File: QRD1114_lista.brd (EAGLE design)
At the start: 66 x 21 mm, 17 parts

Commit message: Add files via upload
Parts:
- removed LED1: (no value), led:CHIPLED-0603-TTW
- added LED: (no value), led:CHIPLED-0603-TTW
- added R11: 330, resistor:R0805
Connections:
- new net N$3: LED.A@1, R11.1
- net +5V: now also R11.2; no longer LED1.A@1
- net GND: now also LED.C@1; no longer LED1.C@1
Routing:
- net N$3: track 0.00 -> 9.73 mm
- net GND: track 72.7 -> 69.3 mm
- net S2: track 22.0 -> 20.8 mm
- net +5V: track 84.0 -> 84.6 mm
- net S1: track 30.1 -> 29.5 mm

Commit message: Add files via upload
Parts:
- LED: device led:CHIPLED-0603-TTW -> led:SML0603
- R11: device resistor:R0805 -> resistor:R0603
- moved R11 5.10 mm to (53.2, 11.0)
- moved R1 3.00 mm to (73.5, 9.00)
- moved R10 3.00 mm to (26.5, 9.00)
- moved R2 3.00 mm to (76.5, 9.00)
- moved R3 3.00 mm to (61.5, 4.00)
- moved R4 3.00 mm to (58.5, 4.00)
- moved R5 3.00 mm to (48.5, 4.00)
- moved R6 3.00 mm to (51.5, 4.00)
- moved R7 3.00 mm to (41.5, 4.00)
- moved R8 3.00 mm to (38.5, 4.00)
- moved R9 3.00 mm to (23.5, 9.00)
- moved LED 0.35 mm to (50.0, 14.2), turned to 0 degrees
- flipped S1 to the bottom
- flipped S2 to the bottom
- flipped S3 to the bottom
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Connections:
- net GND: now also LED.C; no longer LED.C@1
- net N$3: now also LED.A; no longer LED.A@1
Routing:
- net +5V: track 84.6 -> 0.10 mm, vias 2 -> 0
- net GND: track 69.3 -> 0.00 mm, vias 0 -> 1
- net N$3: track 9.73 -> 3.47 mm
- net S2: track 20.8 -> 26.9 mm
- net S4: track 21.6 -> 17.0 mm, vias 2 -> 0
- net S1: track 29.5 -> 34.0 mm, vias 0 -> 1
- net S5: track 27.1 -> 23.4 mm, vias 2 -> 0
- net S3: track 15.7 -> 17.9 mm
- added copper zone on layer 1, net +5V
- added copper zone on layer 16, net GND
- removed copper zone on layer 1, net GND1
- removed copper zone on layer 16, net GND2
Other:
- board size 66 x 21 mm -> 66 x 22 mm
- board text added: "°"

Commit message: Add files via upload
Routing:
- net GND: track 0.00 -> 1.00 mm
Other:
- board text added: "QRD-bar-0,1_version"
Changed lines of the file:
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@@
 <setting verticaltext="up"/>
 </settings>
-<grid distance="1" unitdist="mm" unit="mm" style="lines" multiple="1" display="yes" altdistance="0.25" altunitdist="mm" altunit="mm"/>
+<grid distance="1" unitdist="mm" unit="mm" style="lines" multiple="1" display="yes" altdistance="0.125" altunitdist="mm" altunit="mm"/>
 <layers>
 <layer number="1" name="Top" color="4" fill="1" visible="yes" active="yes"/>
@@
 <text x="44" y="17.25" size="1.778" layer="51" font="vector" rot="R270">S4</text>
 <text x="54.25" y="17.25" size="1.778" layer="51" font="vector" rot="R270">GND</text>
-<text x="43" y="5" size="1.778" layer="38" rot="MR0">°</text>
+<text x="43.25" y="5" size="1.778" layer="38" rot="MR0">°</text>
 <text x="53.25" y="5" size="1.778" layer="38" rot="MR0">°</text>
 <text x="63.25" y="5" size="1.778" layer="38" rot="MR0">°</text>
 <text x="78.25" y="10" size="1.778" layer="38" rot="MR0">°</text>
 <text x="28.25" y="10" size="1.778" layer="38" rot="MR0">°</text>
+<hole x="67.5" y="10" drill="3"/>
+<hole x="32.5" y="10" drill="3"/>
+<text x="70" y="14" size="3" layer="52" rot="MR0">QRD-bar-0,1_version</text>
 </plain>
 <attributes>
@@
 <attribute name="NAME" x="24.766" y="8.524" size="0.8128" layer="25" ratio="18" rot="R270"/>
 <attribute name="OC_FARNELL" value="unknown" x="26.5" y="9" size="1.778" layer="27" rot="R270" display="off"/>
-<attribute name="VALUE" x="25.226" y="11.024" size="0.6096" layer="27" ratio="10" rot="R270"/>
+<attribute name="VALUE" x="24.976" y="11.024" size="0.6096" layer="27" ratio="10" rot="R270"/>
 </element>
 <element name="R2" library="rc-master-smd" package="R0603" value="10 kΩ" x="76.5" y="9" smashed="yes" rot="R90">
@@
 </element>
 <element name="LED" library="led" library_urn="urn:adsk.eagle:library:259" package="SML0603" package3d_urn="urn:adsk.eagle:package:15832/1" value="" x="50" y="14.25" smashed="yes">
-<attribute name="NAME" x="50.77" y="13.865" size="0.6096" layer="25" rot="R180"/>
+<attribute name="NAME" x="50.77" y="14.615" size="0.6096" layer="25" rot="R180"/>
 <attribute name="VALUE" x="51.905" y="12.98" size="1.27" layer="27" rot="R90"/>
 </element>
@@
 <wire x1="26.5" y1="11" x2="26.5" y2="13.2714" width="1.016" layer="1"/>
 <wire x1="26.5" y1="13.2714" x2="26.0414" y2="13.73" width="1.016" layer="1"/>
-<wire x1="26.5" y1="11" x2="28.5" y2="13" width="1.016" layer="1"/>
-<wire x1="34" y1="13" x2="40" y2="19" width="1.016" layer="1"/>
+<wire x1="26.5" y1="11" x2="29.5" y2="14" width="1.016" layer="1"/>
+<wire x1="35" y1="14" x2="40" y2="19" width="1.016" layer="1"/>
 <wire x1="40" y1="19" x2="42.38" y2="19" width="1.016" layer="1"/>
-<wire x1="28.5" y1="13" x2="34" y2="13" width="1.016" layer="1"/>
+<wire x1="29.5" y1="14" x2="35" y2="14" width="1.016" layer="1"/>
 </signal>
 <signal name="S3">
@@
 <wire x1="51.5" y1="4.762" x2="51.5" y2="8.2714" width="1.016" layer="1"/>
 <wire x1="51.5" y1="8.2714" x2="51.0414" y2="8.73" width="1.016" layer="1"/>
-<wire x1="51.0414" y1="8.73" x2="51.3114" y2="9" width="1.016" layer="16"/>
-<wire x1="51.3114" y1="9" x2="52" y2="9" width="1.016" layer="16"/>
-<wire x1="52" y1="9" x2="53" y2="10" width="1.016" layer="16"/>
+<wire x1="51.0414" y1="8.73" x2="51.0614" y2="8.75" width="1.016" layer="16"/>
+<wire x1="51.0614" y1="8.75" x2="51.75" y2="8.75" width="1.016" layer="16"/>
+<wire x1="51.75" y1="8.75" x2="53" y2="10" width="1.016" layer="16"/>
 <wire x1="53" y1="10" x2="53" y2="13" width="1.016" layer="16"/>
 <wire x1="53" y1="13" x2="47.46" y2="18.54" width="1.016" layer="16"/>
@@
 <contactref element="LED" pad="C"/>
 <polygon width="0.254" layer="16">
-<vertex x="83" y="23"/>
-<vertex x="83" y="1"/>
-<vertex x="17" y="1"/>
-<vertex x="17" y="23"/>
+<vertex x="77" y="23"/>
+<vertex x="77" y="1"/>
+<vertex x="23" y="1"/>
+<vertex x="23" y="23"/>
 </polygon>
-<via x="49.25" y="14.25" extent="1-16" drill="0.35"/>
+<wire x1="49.25" y1="14.25" x2="48.25" y2="14.25" width="1.016" layer="1"/>
+<via x="48.25" y="14.25" extent="1-16" drill="0.35"/>
 </signal>
 <signal name="+5V">
@@
 <contactref element="R9" pad="2"/>
 <polygon width="0.254" layer="1">
-<vertex x="17" y="1"/>
-<vertex x="17" y="23"/>
-<vertex x="83" y="23"/>
-<vertex x="83" y="1"/>
+<vertex x="23" y="1"/>
+<vertex x="23" y="23"/>
+<vertex x="77" y="23"/>
+<vertex x="77" y="1"/>
 </polygon>
 <wire x1="73.5" y1="8.238" x2="73.459540625" y2="8.299978125" width="0" layer="19" extent="1-1"/>

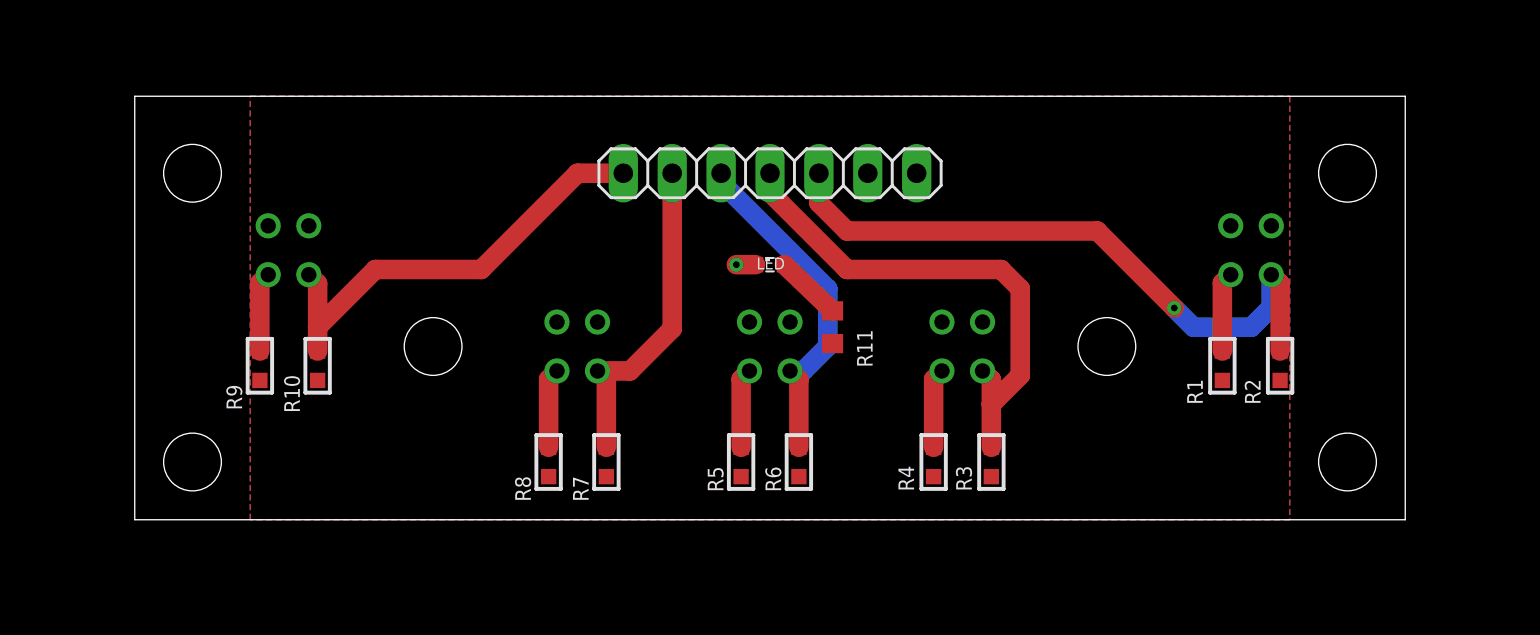
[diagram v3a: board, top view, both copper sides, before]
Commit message: Prepare PCB to manufacturing
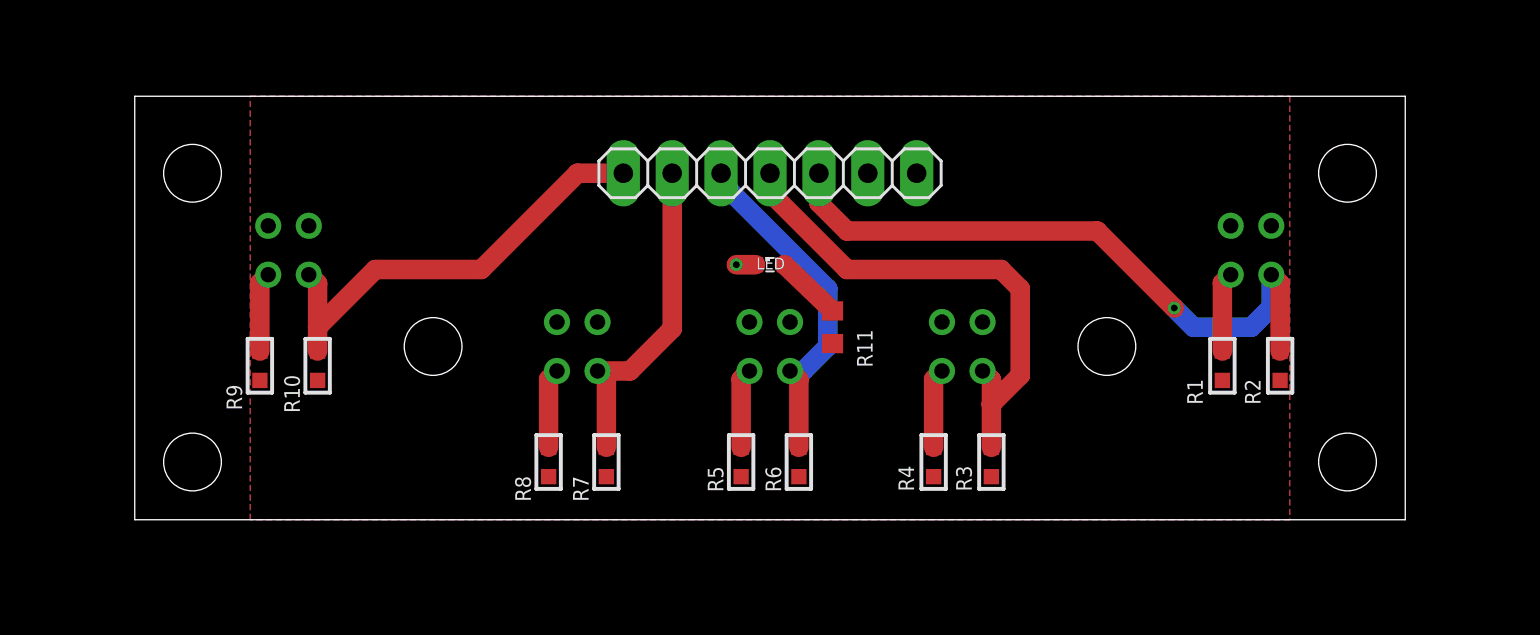
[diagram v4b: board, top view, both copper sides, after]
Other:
- board text added: "QRD1114-bar v1.0"
- board text added: "TVavrinec"
- board text removed: "QRD-bar-0,1_version"
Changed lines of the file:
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@@
 <hole x="67.5" y="10" drill="3"/>
 <hole x="32.5" y="10" drill="3"/>
-<text x="70" y="14" size="3" layer="52" rot="MR0">QRD-bar-0,1_version</text>
+<text x="38.875" y="20.625" size="1.778" layer="51" font="vector" ratio="20">QRD1114-bar v1.0</text>
+<text x="65" y="2" size="1.778" layer="51" font="vector" ratio="20">TVavrinec</text>
 </plain>
 <attributes>
@@
 </class>
 </classes>
-<designrules name="default">
+<designrules name="robotikabrno">
 <description language="de">&lt;b&gt;EAGLE Design Rules&lt;/b&gt;
 &lt;p&gt;
@@
 Einstellungen hier und speichern die Design Rules unter
 einem neuen Namen ab.</description>
-<description language="en">&lt;b&gt;EAGLE Design Rules&lt;/b&gt;
+<description language="en">&lt;b&gt;RobotikaBrno DRC&lt;/b&gt;
 &lt;p&gt;
-The default Design Rules have been set to cover
-a wide range of applications. Your particular design
-may have different requirements, so please make the
-necessary adjustments and save your customized
-design rules under a new name.</description>
+This DRC includes the common parameters for two-layer PCBs. Should be compatible with:
+&lt;ul&gt;
+&lt;li&gt;Gatema POOL Servis&lt;/li&gt;
+&lt;li&gt;JLCPCB (no extras)&lt;/li&gt;
+&lt;li&gt;AllPCB (no extras)&lt;/li&gt;
+&lt;/ul&gt;</description>
 <param name="layerSetup" value="(1*16)"/>
 <param name="mtCopper" value="0.035mm 0.035mm 0.035mm 0.035mm 0.035mm 0.035mm 0.035mm 0.035mm 0.035mm 0.035mm 0.035mm 0.035mm 0.035mm 0.035mm 0.035mm 0.035mm"/>
 <param name="mtIsolate" value="1.5mm 0.15mm 0.2mm 0.15mm 0.2mm 0.15mm 0.2mm 0.15mm 0.2mm 0.15mm 0.2mm 0.15mm 0.2mm 0.15mm 0.2mm"/>
-<param name="mdWireWire" value="6mil"/>
-<param name="mdWirePad" value="6mil"/>
-<param name="mdWireVia" value="6mil"/>
-<param name="mdPadPad" value="6mil"/>
-<param name="mdPadVia" value="6mil"/>
-<param name="mdViaVia" value="6mil"/>
-<param name="mdSmdPad" value="6mil"/>
-<param name="mdSmdVia" value="6mil"/>
-<param name="mdSmdSmd" value="6mil"/>
+<param name="mdWireWire" value="0.2mm"/>
+<param name="mdWirePad" value="0.2mm"/>
+<param name="mdWireVia" value="0.2mm"/>
+<param name="mdPadPad" value="0.2mm"/>
+<param name="mdPadVia" value="0.2mm"/>
+<param name="mdViaVia" value="0.2mm"/>
+<param name="mdSmdPad" value="0.2mm"/>
+<param name="mdSmdVia" value="0.2mm"/>
+<param name="mdSmdSmd" value="0.2mm"/>
 <param name="mdViaViaSameLayer" value="6mil"/>
 <param name="mnLayersViaInSmd" value="2"/>
-<param name="mdCopperDimension" value="40mil"/>
-<param name="mdDrill" value="6mil"/>
+<param name="mdCopperDimension" value="0.5mm"/>
+<param name="mdDrill" value="0.5mm"/>
 <param name="mdSmdStop" value="0mil"/>
-<param name="msWidth" value="6mil"/>
+<param name="msWidth" value="0.2mm"/>
 <param name="msDrill" value="0.35mm"/>
 <param name="msMicroVia" value="9.99mm"/>
 <param name="msBlindViaRatio" value="0.5"/>
-<param name="rvPadTop" value="0.25"/>
-<param name="rvPadInner" value="0.25"/>
-<param name="rvPadBottom" value="0.25"/>
-<param name="rvViaOuter" value="0.25"/>
-<param name="rvViaInner" value="0.25"/>
+<param name="rvPadTop" value="0.35"/>
+<param name="rvPadInner" value="0.35"/>
+<param name="rvPadBottom" value="0.35"/>
+<param name="rvViaOuter" value="0.35"/>
+<param name="rvViaInner" value="0.35"/>
 <param name="rvMicroViaOuter" value="0.25"/>
 <param name="rvMicroViaInner" value="0.25"/>
-<param name="rlMinPadTop" value="10mil"/>
-<param name="rlMaxPadTop" value="20mil"/>
-<param name="rlMinPadInner" value="10mil"/>
-<param name="rlMaxPadInner" value="20mil"/>
-<param name="rlMinPadBottom" value="10mil"/>
-<param name="rlMaxPadBottom" value="20mil"/>
-<param name="rlMinViaOuter" value="8mil"/>
-<param name="rlMaxViaOuter" value="20mil"/>
-<param name="rlMinViaInner" value="8mil"/>
-<param name="rlMaxViaInner" value="20mil"/>
+<param name="rlMinPadTop" value="0.16mm"/>
+<param name="rlMaxPadTop" value="1mm"/>
+<param name="rlMinPadInner" value="0.16mm"/>
+<param name="rlMaxPadInner" value="1mm"/>
+<param name="rlMinPadBottom" value="0.16mm"/>
+<param name="rlMaxPadBottom" value="1mm"/>
+<param name="rlMinViaOuter" value="0.16mm"/>
+<param name="rlMaxViaOuter" value="1mm"/>
+<param name="rlMinViaInner" value="0.16mm"/>
+<param name="rlMaxViaInner" value="1mm"/>
 <param name="rlMinMicroViaOuter" value="4mil"/>
 <param name="rlMaxMicroViaOuter" value="20mil"/>
 <param name="rlMinMicroViaInner" value="4mil"/>
 <param name="rlMaxMicroViaInner" value="20mil"/>
-<param name="psTop" value="-1"/>
-<param name="psBottom" value="-1"/>
-<param name="psFirst" value="-1"/>
+<param name="psTop" value="1"/>
+<param name="psBottom" value="1"/>
+<param name="psFirst" value="1"/>
 <param name="psElongationLong" value="100"/>
 <param name="psElongationOffset" value="100"/>
-<param name="mvStopFrame" value="1"/>
+<param name="mvStopFrame" value="0.1"/>
 <param name="mvCreamFrame" value="0"/>
-<param name="mlMinStopFrame" value="4mil"/>
-<param name="mlMaxStopFrame" value="4mil"/>
+<param name="mlMinStopFrame" value="0.1mm"/>
+<param name="mlMaxStopFrame" value="0.2mm"/>
 <param name="mlMinCreamFrame" value="0mil"/>
 <param name="mlMaxCreamFrame" value="0mil"/>
-<param name="mlViaStopLimit" value="0mil"/>
+<param name="mlViaStopLimit" value="0.4mm"/>
 <param name="srRoundness" value="0"/>
 <param name="srMinRoundness" value="0mil"/>
 <param name="srMaxRoundness" value="0mil"/>
-<param name="slThermalIsolate" value="10mil"/>
+<param name="slThermalIsolate" value="0.2mm"/>
 <param name="slThermalsForVias" value="0"/>
 <param name="dpMaxLengthDifference" value="10mm"/>
@@
 <contactref element="R5" pad="2"/>
 <contactref element="JP1" pad="2"/>
-<wire x1="73.406" y1="8.382" x2="73.459540625" y2="8.299978125" width="0.254" layer="1"/>
 <contactref element="R11" pad="2"/>
 <contactref element="R10" pad="2"/>
@@
 <vertex x="77" y="1"/>
 </polygon>
-<wire x1="73.5" y1="8.238" x2="73.459540625" y2="8.299978125" width="0" layer="19" extent="1-1"/>
 </signal>
 <signal name="N$7">
